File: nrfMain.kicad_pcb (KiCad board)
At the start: 2 copper layers, 3 parts, among them J1 FTSH-105-01-F-DV-P-TR, U1 nRF52840

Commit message: Setup charging
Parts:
- added J2: USB_C_Receptacle, Connector_USB:USB_C_Receptacle_GCT_USB4105-xx-A_16P_TopMnt_Horizontal, F.Cu at (75.7, 46.4)
- added Y1: 32MHz, Crystal:Crystal_SMD_HC49-SD, F.Cu at (77.2, 32.7)
- added Y2: 32.768kHz, Crystal:Crystal_SMD_3215-2Pin_3.2x1.5mm, F.Cu at (72.4, 37.5)
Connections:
- AE1 pad 1: Net-(U1-ANT) -> Net-(AE1-Pad1)
- U1 pad AD4: unconnected-(U1-D--PadAD4) -> D-
- U1 pad AD6: unconnected-(U1-D+-PadAD6) -> D+
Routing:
- net GND: track 9.40 -> 1.21 mm
- net Net-(U1-ANT): track 3.59 -> 0.00 mm

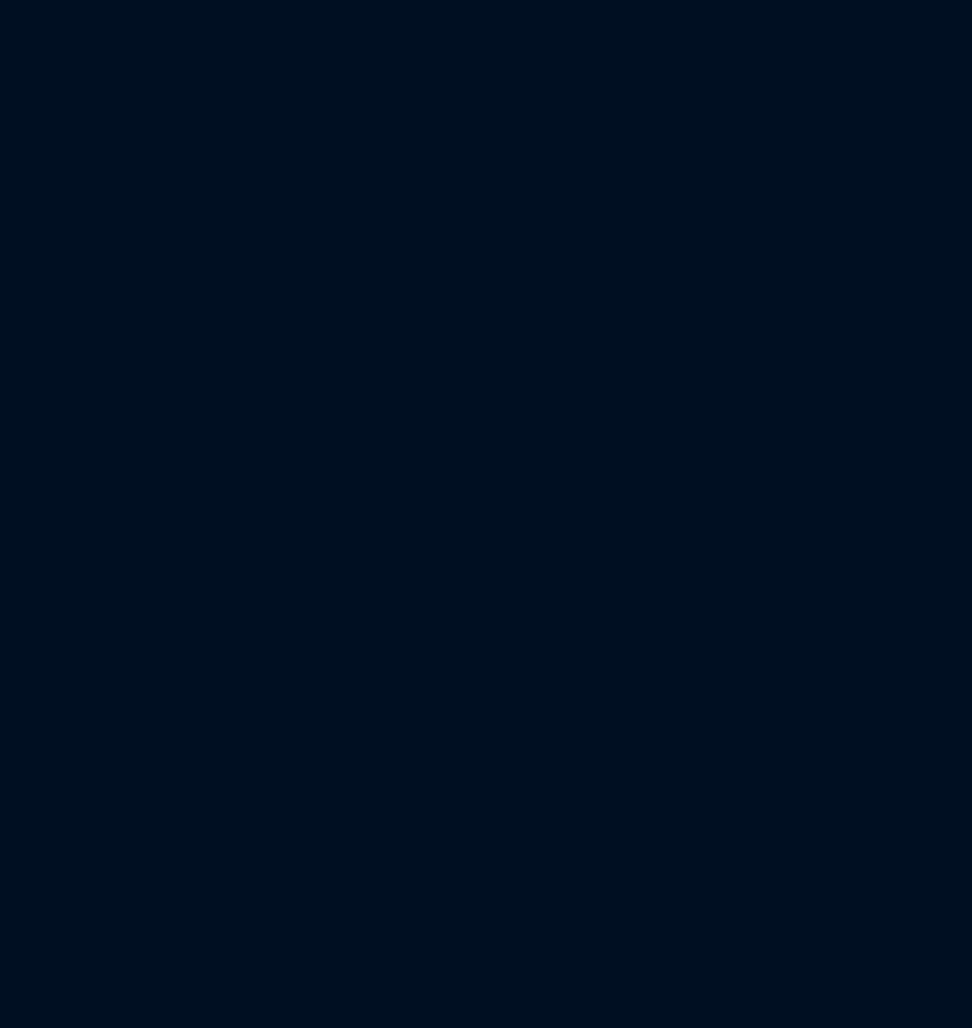
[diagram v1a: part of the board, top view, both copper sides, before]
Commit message: Added output headers
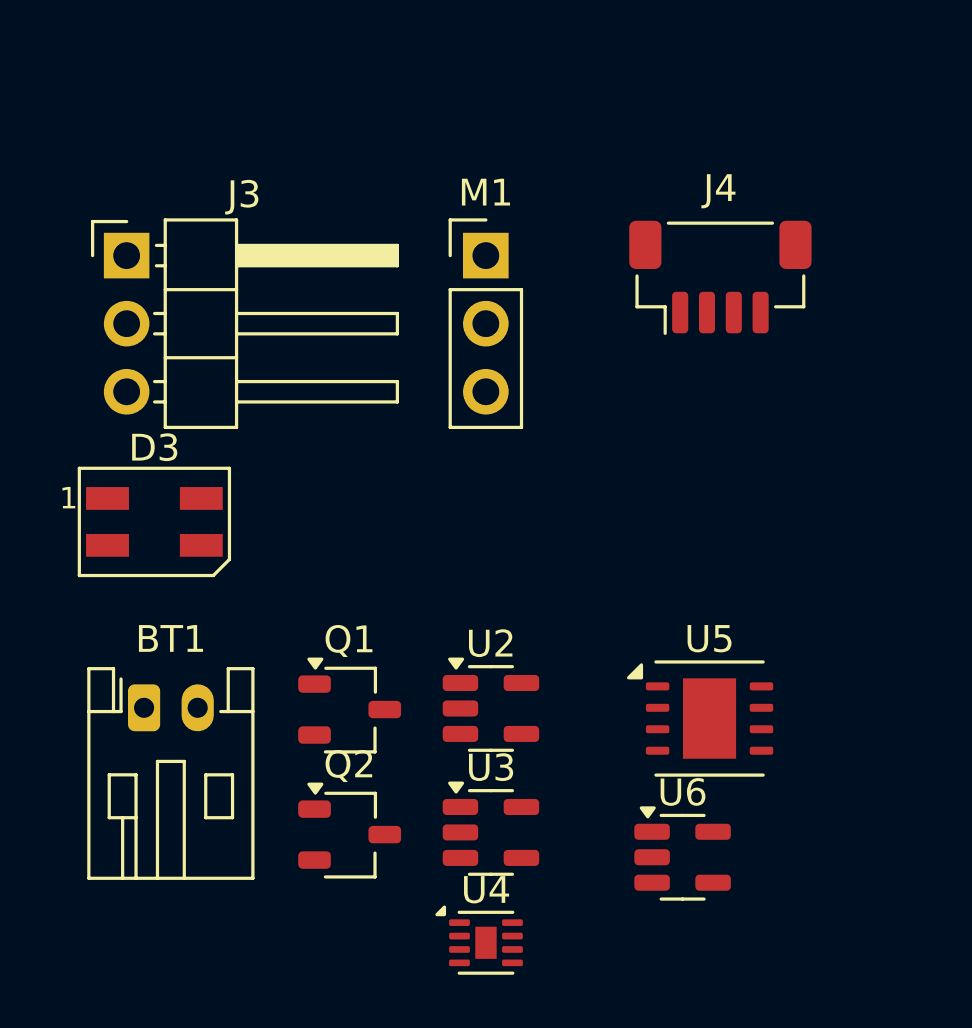
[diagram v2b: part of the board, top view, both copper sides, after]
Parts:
- added BT1: Battery_Cell, Connector_JST:JST_PH_S2B-PH-K_1x02_P2.00mm_Horizontal, F.Cu at (53.3, 78.0)
- added D3: SK6812MINI, LED_SMD:LED_SK6812MINI_PLCC4_3.5x3.5mm_P1.75mm, F.Cu at (53.7, 71.0)
- added J3: Conn_01x03, Connector_PinHeader_2.54mm:PinHeader_1x03_P2.54mm_Horizontal, F.Cu at (52.6, 61.1)
- added J4: Conn_01x04, Connector_JST:JST_SH_BM04B-SRSS-TB_1x04-1MP_P1.00mm_Vertical, F.Cu at (74.8, 61.9)
- added M1: Motor_Servo, Connector_PinHeader_2.54mm:PinHeader_1x03_P2.54mm_Vertical, F.Cu at (66.0, 61.1)
- added Q1: Q_NMOS_GSD, Package_TO_SOT_SMD:TSOT-23, F.Cu at (60.9, 78.0)
- added Q2: Q_NMOS_GSD, Package_TO_SOT_SMD:TSOT-23, F.Cu at (60.9, 82.7)
- added U2: ~, Package_TO_SOT_SMD:SOT-23-5, F.Cu at (66.2, 78.0)
- added U3: MCP73831-2-OT, Package_TO_SOT_SMD:SOT-23-5, F.Cu at (66.2, 82.6)
- added U4: MAX17048, Package_DFN_QFN:TDFN-8-1EP_2x2mm_P0.5mm_EP0.8x1.2mm, F.Cu at (66.0, 86.7)
- added U5: MX25R6435FZAIL0, Package_SON:WSON-8-1EP_4x4mm_P0.8mm_EP1.98x3mm, F.Cu at (74.4, 78.4)
- added U6: AP22814AW5, Package_TO_SOT_SMD:SOT-23-5, F.Cu at (73.4, 83.5)
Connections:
- J1 pad 01: unconnected-(J1-Pad01) -> +3.3V
- J1 pad 02: unconnected-(J1-Pad02) -> Net-(U1-SWDIO)
- J1 pad 03: unconnected-(J1-Pad03) -> GND
- J1 pad 04: unconnected-(J1-Pad04) -> Net-(U1-SWDCLK)
- J1 pad 05: unconnected-(J1-Pad05) -> GND
- J1 pad 06: unconnected-(J1-Pad06) -> /MCU/SWO
- J1 pad 09: unconnected-(J1-Pad09) -> GND
- J1 pad 10: unconnected-(J1-Pad10) -> Net-(U1-P0.18/~{RESET})
- J2 pad A1: Net-(J2-GND-PadA1) -> GND
- J2 pad A12: Net-(J2-GND-PadA1) -> GND
- J2 pad A4: Net-(J2-VBUS-PadA4) -> VBUS
- J2 pad A5: unconnected-(J2-CC1-PadA5) -> Net-(J2-CC1)
- J2 pad A9: Net-(J2-VBUS-PadA4) -> VBUS
- J2 pad B1: Net-(J2-GND-PadA1) -> GND
- J2 pad B12: Net-(J2-GND-PadA1) -> GND
- J2 pad B4: Net-(J2-VBUS-PadA4) -> VBUS
- J2 pad B5: unconnected-(J2-CC2-PadB5) -> Net-(J2-CC2)
- J2 pad B9: Net-(J2-VBUS-PadA4) -> VBUS
- U1 pad A12: unconnected-(U1-AIN0/P0.02-PadA12) -> A_BAT
- U1 pad A22: Net-(U1-VDD-PadA22) -> +3.3V
- U1 pad A23: unconnected-(U1-XC2-PadA23) -> Net-(U1-XC2)
- U1 pad AA24: unconnected-(U1-SWDCLK-PadAA24) -> Net-(U1-SWDCLK)
- U1 pad AC13: unconnected-(U1-P0.18/~{RESET}-PadAC13) -> Net-(U1-P0.18/~{RESET})
- U1 pad AC15: unconnected-(U1-P0.19-PadAC15) -> /MCU/QSPI_SCK
- U1 pad AC17: unconnected-(U1-P0.21-PadAC17) -> /MCU/QSPI_SIO1
- U1 pad AC19: unconnected-(U1-P0.23-PadAC19) -> /MCU/QSPI_SIO3
- U1 pad AC24: unconnected-(U1-SWDIO-PadAC24) -> Net-(U1-SWDIO)
- U1 pad AC5: unconnected-(U1-DECUSB-PadAC5) -> Net-(U1-DECUSB)
- U1 pad AD12: unconnected-(U1-P0.17-PadAD12) -> /MCU/QSPI_CS
- U1 pad AD14: Net-(U1-VDD-PadA22) -> +3.3V
- U1 pad AD16: unconnected-(U1-P0.20-PadAD16) -> /MCU/QSPI_SIO0
- U1 pad AD18: unconnected-(U1-P0.22-PadAD18) -> /MCU/QSPI_SIO2
- U1 pad AD2: unconnected-(U1-VBUS-PadAD2) -> VBUS
- U1 pad AD22: unconnected-(U1-TRACEDATA0/P1.00-PadAD22) -> /MCU/SWO
- U1 pad AD23: Net-(U1-VDD-PadA22) -> +3.3V
- U1 pad B1: Net-(U1-VDD-PadA22) -> +3.3V
- U1 pad B13: unconnected-(U1-AIN1/P0.03-PadB13) -> /MCU/Perf_enable
- U1 pad B24: unconnected-(U1-XC1-PadB24) -> Net-(U1-XC1)
- U1 pad B5: unconnected-(U1-DEC4-PadB5) -> Net-(U1-DEC4)
- U1 pad C1: unconnected-(U1-DEC1-PadC1) -> Net-(U1-DEC1)
- U1 pad D2: unconnected-(U1-XL1/P0.00-PadD2) -> Net-(U1-XL1/P0.00)
- U1 pad D23: unconnected-(U1-DEC3-PadD23) -> Net-(U1-DEC3)
- U1 pad E24: unconnected-(U1-DEC6-PadE24) -> Net-(U1-DEC4)
- U1 pad F2: unconnected-(U1-XL2/P0.01-PadF2) -> Net-(U1-XL2/P0.01)
- U1 pad F23: unconnected-(U1-VSS_PA-PadF23) -> GND
- U1 pad G1: unconnected-(U1-P0.26-PadG1) -> SDA
- U1 pad H2: unconnected-(U1-P0.27-PadH2) -> SCL
- U1 pad J1: unconnected-(U1-AIN2/P0.04-PadJ1) -> BAT_IND
- U1 pad K2: unconnected-(U1-AIN3/P0.05-PadK2) -> LED
- U1 pad W1: Net-(U1-VDD-PadA22) -> +3.3V
- U1 pad Y2: unconnected-(U1-VDDH-PadY2) -> +3.3V
- Y1 pad 1: unconnected-(Y1-Pad1) -> Net-(U1-XC2)
- Y1 pad 2: unconnected-(Y1-Pad2) -> Net-(U1-XC1)
- Y2 pad 1: unconnected-(Y2-Pad1) -> Net-(U1-XL2/P0.01)
- Y2 pad 2: unconnected-(Y2-Pad2) -> Net-(U1-XL1/P0.00)

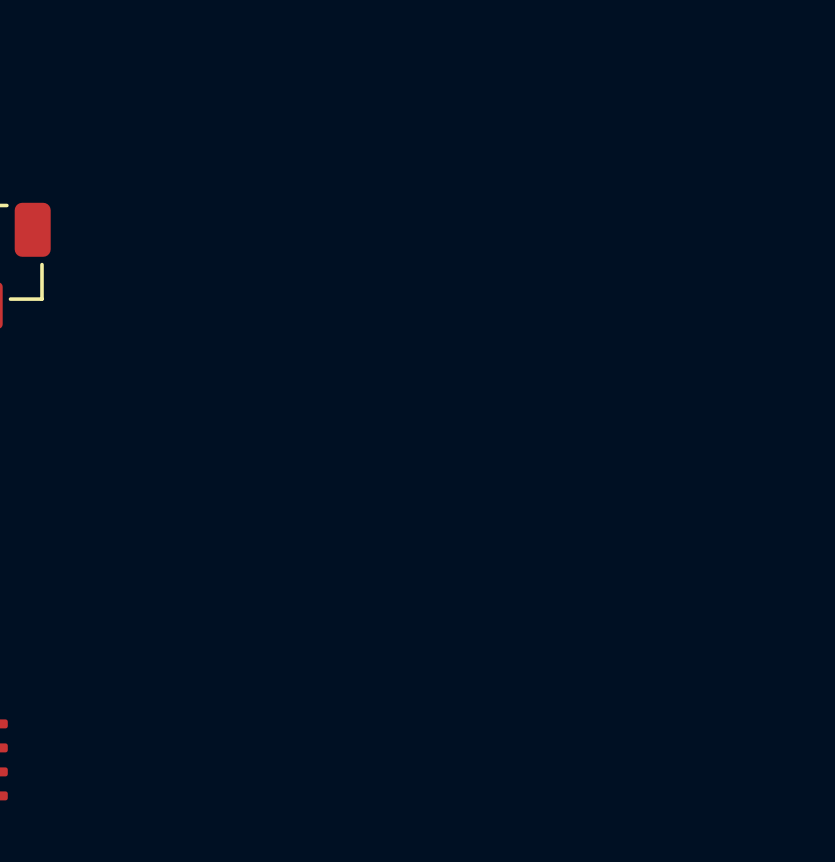
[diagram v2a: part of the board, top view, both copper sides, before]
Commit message: Added impedance match, gitignore
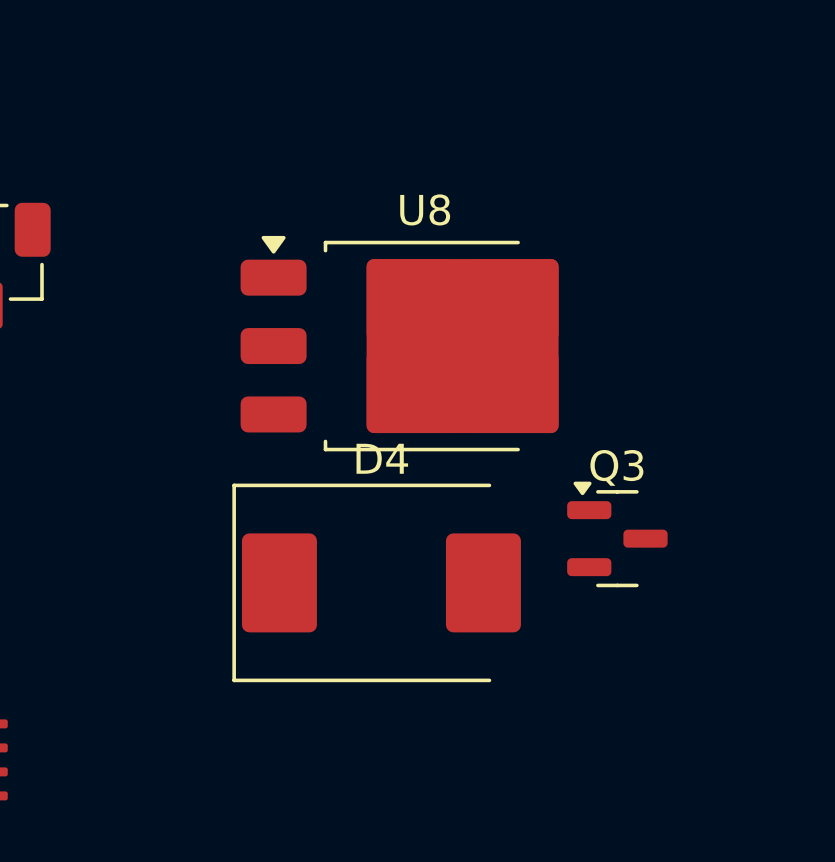
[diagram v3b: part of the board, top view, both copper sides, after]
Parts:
- added D4: B340, Diode_SMD:D_SMC, F.Cu at (89.2, 72.5)
- added Q3: DMG2301L, Package_TO_SOT_SMD:SOT-23, F.Cu at (97.1, 71.0)
- added U8: LD39150DT33, Package_TO_SOT_SMD:TO-252-3_TabPin2, F.Cu at (90.6, 64.6)

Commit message: finished schematic
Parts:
- added C1: 12p, Capacitor_SMD:C_0603_1608Metric, F.Cu at (128.9, 39.7)
- added C10: .1u, Capacitor_SMD:C_0603_1608Metric, F.Cu at (110.5, 47.3)
- added C11: 1u, Capacitor_SMD:C_0603_1608Metric, F.Cu at (128.9, 54.8)
- added C12: .1u, Capacitor_SMD:C_0603_1608Metric, F.Cu at (133.0, 39.7)
- added C13: .1u, Capacitor_SMD:C_0603_1608Metric, F.Cu at (133.0, 42.2)
- added C14: 4.7u, Capacitor_SMD:C_0603_1608Metric, F.Cu at (133.0, 44.8)
- added C15: 4.7u, Capacitor_SMD:C_0603_1608Metric, F.Cu at (133.0, 47.3)
- added C16: .1u, Capacitor_SMD:C_0603_1608Metric, F.Cu at (133.0, 49.8)
- added C17: 1u, Capacitor_SMD:C_0603_1608Metric, F.Cu at (133.0, 52.3)
- added C18: 100p, Capacitor_SMD:C_0603_1608Metric, F.Cu at (133.0, 54.8)
- added C19: 1u, Capacitor_SMD:C_0603_1608Metric, F.Cu at (110.5, 49.8)
- added C2: 12p, Capacitor_SMD:C_0603_1608Metric, F.Cu at (128.9, 42.2)
- added C20: 1u, Capacitor_SMD:C_0603_1608Metric, F.Cu at (110.5, 52.3)
- added C21: 2.4p, Capacitor_SMD:C_0603_1608Metric, F.Cu at (137.0, 39.7)
- added C22: 2.4p, Capacitor_SMD:C_0603_1608Metric, F.Cu at (137.0, 42.2)
- added C23: .1u, Capacitor_SMD:C_0603_1608Metric, F.Cu at (135.7, 33.2)
- added C3: 12p, Capacitor_SMD:C_0603_1608Metric, F.Cu at (128.9, 44.8)
- added C4: 12p, Capacitor_SMD:C_0603_1608Metric, F.Cu at (128.9, 47.3)
- added C5: 0.5p, Capacitor_SMD:C_0603_1608Metric, F.Cu at (128.9, 49.8)
- added C6: 0.8p, Capacitor_SMD:C_0603_1608Metric, F.Cu at (128.9, 52.3)
- added C7: .1u, Capacitor_SMD:C_0603_1608Metric, F.Cu at (110.5, 39.7)
- added C8: 4.7u, Capacitor_SMD:C_0603_1608Metric, F.Cu at (110.5, 42.2)
- added C9: 4.7u, Capacitor_SMD:C_0603_1608Metric, F.Cu at (110.5, 44.8)
- added D1: B340, Diode_SMD:D_SMC, F.Cu at (113.9, 57.4)
- added D2: LED, LED_SMD:LED_0805_2012Metric, F.Cu at (121.6, 59.3)
- added D5: D_TVS, Diode_SMD:D_0402_1005Metric, F.Cu at (122.2, 39.5)
- added F1: Fuse, Fuse:Fuse_1210_3225Metric, F.Cu at (122.1, 55.6)
- added J5: 2337019-1, Personal:TE_2337019-1, F.Cu at (141.8, 49.4)
- added L1: 4.7n, Inductor_SMD:L_0603_1608Metric, F.Cu at (137.0, 44.8)
- added L2: 2.4n, Inductor_SMD:L_0603_1608Metric, F.Cu at (137.0, 47.3)
- added M2: Motor_Servo, Connector_PinHeader_2.54mm:PinHeader_1x03_P2.54mm_Vertical, F.Cu at (88.9, 73.7)
- added M3: Motor_Servo, Connector_PinHeader_2.54mm:PinHeader_1x03_P2.54mm_Vertical, F.Cu at (93.5, 73.7)
- added M4: Motor_Servo, Connector_PinHeader_2.54mm:PinHeader_1x03_P2.54mm_Vertical, F.Cu at (98.2, 73.7)
- added M5: Motor_Servo, Connector_PinHeader_2.54mm:PinHeader_1x03_P2.54mm_Vertical, F.Cu at (102.8, 73.7)
- added M6: Motor_Servo, Connector_PinHeader_2.54mm:PinHeader_1x03_P2.54mm_Vertical, F.Cu at (107.5, 73.7)
- added MK2: MMICT390200012, Sensor_Audio:Knowles_LGA-5_3.5x2.65mm, F.Cu at (101.2, 88.6)
- added R1: 5.1k, Resistor_SMD:R_0603_1608Metric, F.Cu at (114.5, 39.7)
- added R10: 10k, Resistor_SMD:R_0603_1608Metric, F.Cu at (137.0, 49.8)
- added R2: 5.1k, Resistor_SMD:R_0603_1608Metric, F.Cu at (114.5, 42.2)
- added R3: 220, Resistor_SMD:R_0603_1608Metric, F.Cu at (114.5, 44.8)
- added R4: 2k, Resistor_SMD:R_0603_1608Metric, F.Cu at (114.5, 47.3)
- added R5: 2k, Resistor_SMD:R_0603_1608Metric, F.Cu at (114.5, 49.8)
- added R6: 470, Resistor_SMD:R_0603_1608Metric, F.Cu at (114.5, 52.3)
- added R7: 100k, Resistor_SMD:R_0603_1608Metric, F.Cu at (118.5, 39.7)
- added R8: 100k, Resistor_SMD:R_0603_1608Metric, F.Cu at (118.5, 42.2)
- added R9: 100k, Resistor_SMD:R_0603_1608Metric, F.Cu at (118.5, 44.8)
- added SW1: SW_Push, Button_Switch_THT:SW_PUSH_6mm, F.Cu at (82.0, 107.0)
- moved Q1 113.0 mm to (173.6, 69.1)
- moved Q2 113.0 mm to (173.6, 73.8)
- moved U2 113.0 mm to (178.9, 69.0)
- moved U3 113.0 mm to (178.9, 73.7)
- moved U4 113.0 mm to (178.7, 77.8)
- moved U6 113.0 mm to (186.0, 74.6)
- moved J2 81.8 mm to (105.0, 122.8)
- moved BT1 74.8 mm to (119.8, 112.2), turned to 90 degrees
- moved J3 62.1 mm to (113.0, 75.6), turned to 90 degrees
- moved AE1 61.2 mm to (72.6, 99.1), turned to 90 degrees
- moved D3 57.5 mm to (84.8, 119.4)
- moved J1 57.3 mm to (115.0, 102.5)
- moved Y1 55.0 mm to (87.2, 86.8)
- moved J4 53.2 mm to (118.5, 92.2), turned to -90 degrees
- moved U1 49.8 mm to (86.0, 97.5)
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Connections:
- U1 pad A8: unconnected-(U1-AIN7/P0.31-PadA8) -> PDM_DAT
- U1 pad AC11: unconnected-(U1-P0.16-PadAC11) -> PWM_4
- U1 pad AC9: unconnected-(U1-P0.14-PadAC9) -> PWM_2
- U1 pad AD10: unconnected-(U1-P0.15-PadAD10) -> PWM_3
- U1 pad AD20: unconnected-(U1-P0.24-PadAD20) -> PWM_5
- U1 pad AD8: unconnected-(U1-P0.13-PadAD8) -> PWM_1
- U1 pad B9: unconnected-(U1-AIN6/P0.30-PadB9) -> PDM_CLK
- U1 pad L1: unconnected-(U1-P0.06-PadL1) -> Net-(U1-P0.06)
- U1 pad N1: unconnected-(U1-P0.08-PadN1) -> PWM_0

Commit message: PCB layout
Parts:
- added C24: .1u, Capacitor_SMD:C_0603_1608Metric, F.Cu at (83.5, 81.5)
- added C25: 1u, Capacitor_SMD:C_0603_1608Metric, F.Cu at (93.0, 95.0)
- added R11: 10k, Resistor_SMD:R_0603_1608Metric, F.Cu at (95.7, 99.8)
- added R12: 10k, Resistor_SMD:R_0603_1608Metric, F.Cu at (95.7, 101.5)
- added R13: 100k, Resistor_SMD:R_0603_1608Metric, F.Cu at (96.0, 95.0)
- moved U3 117.7 mm to (70.2, 118.9), turned to -90 degrees
- moved D5 107.5 mm to (60.5, 127.5)
- moved U2 106.3 mm to (86.2, 121.3)
- moved U4 104.3 mm to (81.0, 114.2), turned to 90 degrees
- moved R1 101.7 mm to (63.0, 127.5), turned to 180 degrees
- moved U6 99.0 mm to (87.5, 84.9), turned to -90 degrees
- moved R2 97.0 mm to (67.8, 127.2)
- moved Q1 96.4 mm to (91.7, 120.0)
- moved Q2 96.0 mm to (91.7, 123.8)
- moved C21 91.9 mm to (64.5, 96.2), turned to 90 degrees
- moved R7 88.6 mm to (79.5, 119.2), turned to 180 degrees
- moved C9 88.2 mm to (69.2, 122.7), turned to -90 degrees
- moved R8 88.1 mm to (75.8, 119.2), turned to 180 degrees
- moved C7 88.0 mm to (84.2, 123.8)
- moved R3 87.1 mm to (83.0, 126.0), turned to -90 degrees
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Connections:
- net D+ renamed D_P
- net D- renamed D_N
- R10 pad 2: Net-(U1-P0.06) -> Net-(R10-Pad2)
- R7 pad 1: +BATT -> Net-(U2-VDD)
- SW1 pad 1: Net-(U1-P0.06) -> Net-(R10-Pad2)
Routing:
- net +3.3V: track 0.00 -> 101.8 mm, vias 0 -> 12
- net GND: track 0.75 -> 85.4 mm, vias 0 -> 39
- net VBUS: track 0.00 -> 77.7 mm, vias 0 -> 4
- net PWM_0: track 0.00 -> 63.6 mm, vias 0 -> 2
- net SDA: track 0.00 -> 53.0 mm, vias 0 -> 4
- net SCL: track 0.00 -> 49.2 mm, vias 0 -> 5
- net PWM_2: track 0.00 -> 39.5 mm, vias 0 -> 1
- net PWM_1: track 0.00 -> 37.3 mm, vias 0 -> 2
- net PWM_3: track 0.00 -> 28.8 mm, vias 0 -> 1
- net Net-(D4-K): track 0.00 -> 26.6 mm
- net A_BAT: track 0.00 -> 25.0 mm, vias 0 -> 2
- net PWM_4: track 0.00 -> 24.8 mm, vias 0 -> 2
- net LED: track 0.00 -> 24.6 mm, vias 0 -> 1
- net PDM_DAT: track 0.00 -> 23.3 mm, vias 0 -> 2
- net PDM_CLK: track 0.00 -> 23.1 mm, vias 0 -> 2
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- added copper zone on F.Cu, net +3.3V
- added copper zone on F.Cu, net +BATT
- added copper zone on F.Cu, net -BATT
- added copper zone on F.Cu, net GND
- added copper zone on In1.Cu, net GND
- added copper zone on In2.Cu, net GND
- added copper zone on F.Cu, net Net-(BT1--)
- added copper zone on F.Cu, net Net-(D4-K)
- added copper zone on F.Cu, net Net-(Q1-D)
- added copper zone on F.Cu, net VDD
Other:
- board outline added: 40 x 68.8 mm
- copper layers 2 -> 4
